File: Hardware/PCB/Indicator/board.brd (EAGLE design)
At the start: 15 x 18 mm, 9 parts

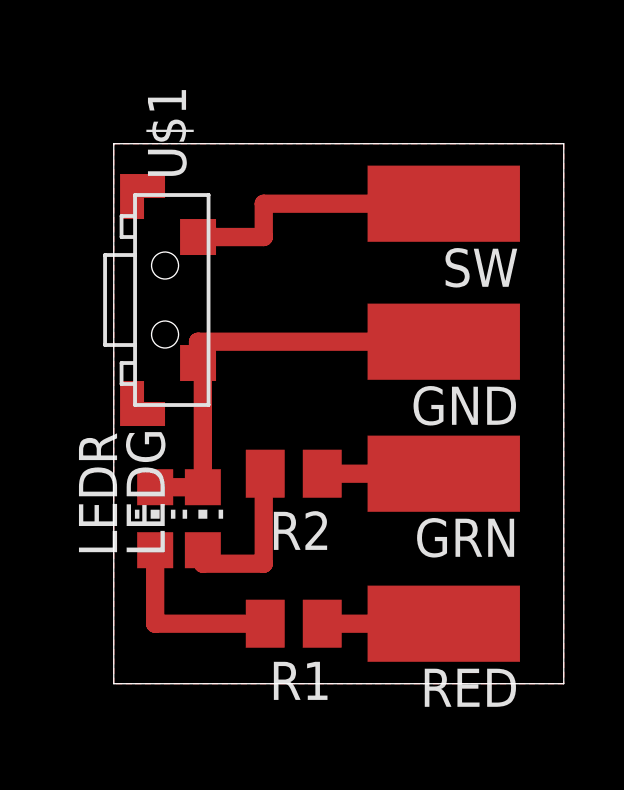
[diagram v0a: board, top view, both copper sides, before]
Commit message: cloud push
- PCB size & pattern modified
- Enclosure minor fix
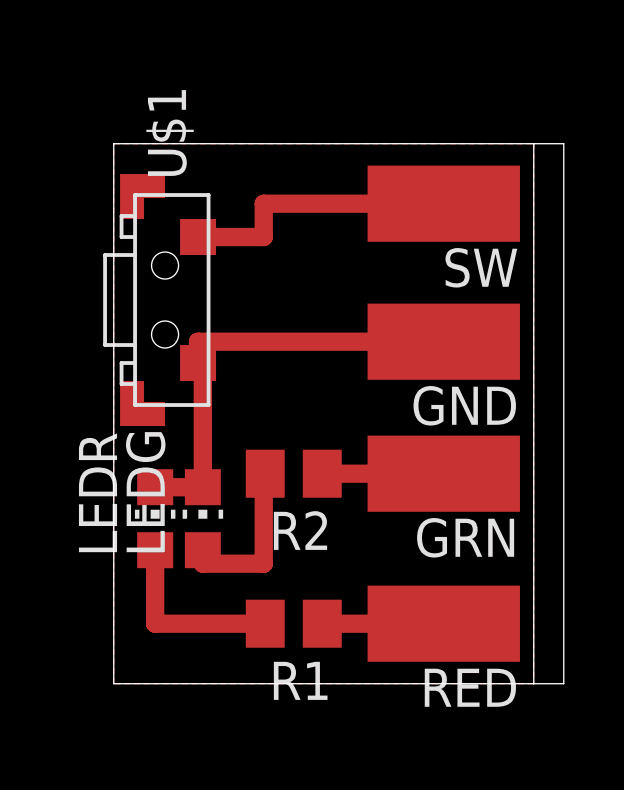
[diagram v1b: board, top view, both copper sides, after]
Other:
- outline, holes or cut-outs redrawn
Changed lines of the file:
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@@
 <board>
 <plain>
-<wire x1="0" y1="0" x2="15" y2="0" width="0" layer="20"/>
-<wire x1="15" y1="0" x2="15" y2="18" width="0" layer="20"/>
-<wire x1="15" y1="18" x2="0" y2="18" width="0" layer="20"/>
+<wire x1="0" y1="0" x2="14" y2="0" width="0" layer="20"/>
+<wire x1="14" y1="0" x2="14" y2="18" width="0" layer="20"/>
+<wire x1="14" y1="18" x2="0" y2="18" width="0" layer="20"/>
 <wire x1="0" y1="18" x2="0" y2="0" width="0" layer="20"/>
+<wire x1="14" y1="18" x2="15" y2="18" width="0" layer="20"/>
+<wire x1="15" y1="18" x2="15" y2="0" width="0" layer="20"/>
+<wire x1="15" y1="0" x2="14" y2="0" width="0" layer="20"/>
 </plain>
 <attributes>
@@
 <wire x1="2.97" y1="10.69" x2="2.97" y2="6.55" width="0.6096" layer="1"/>
 <wire x1="2.97" y1="6.55" x2="1.38" y2="6.55" width="0.6096" layer="1"/>
-<polygon width="0.3048" layer="1" isolate="0.8128" orphans="yes">
+<polygon width="0.3048" layer="1" isolate="0.85">
 <vertex x="0" y="18"/>
-<vertex x="15" y="18"/>
-<vertex x="15" y="0"/>
+<vertex x="14" y="18"/>
+<vertex x="14" y="0"/>
 <vertex x="0" y="0"/>
 </polygon>
